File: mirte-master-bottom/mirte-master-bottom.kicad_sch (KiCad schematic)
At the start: 17 parts, among them J13 oled_conn, J23 e-stop, J6 ledstrip, Q1 DMG2305UX, SW2 EM_SWITCH

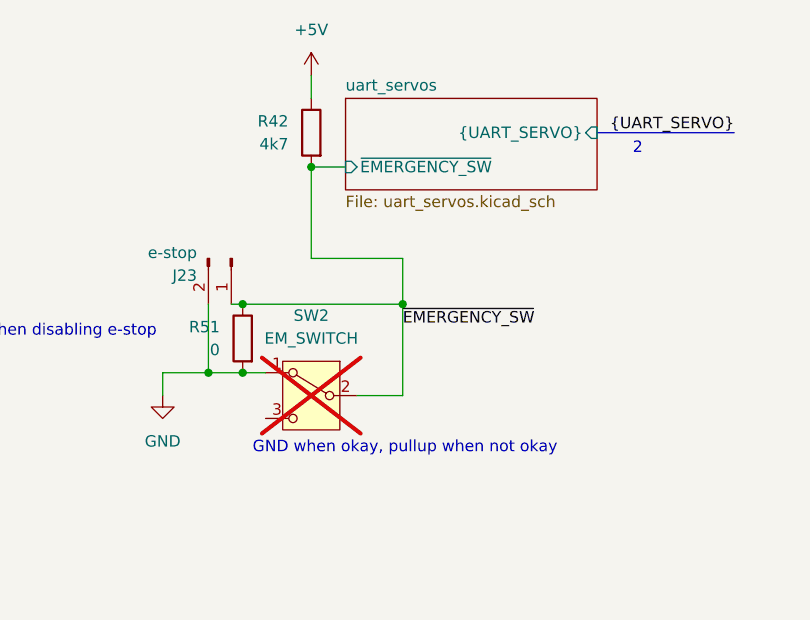
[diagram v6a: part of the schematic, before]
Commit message: change to 12v em switch
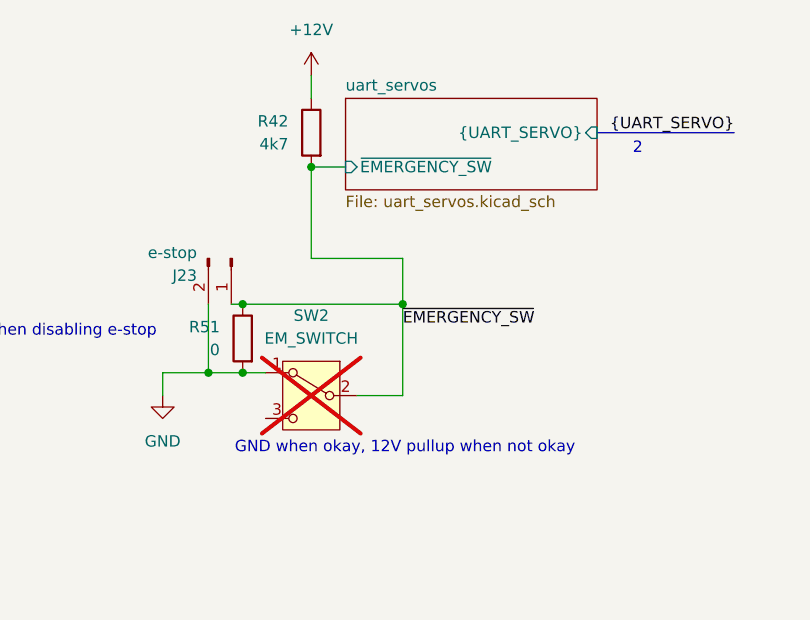
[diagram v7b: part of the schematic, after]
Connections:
- net +12V: now also R42.1
- net +5V: no longer R42.1
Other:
- note added: "GND when okay, 12V pullup when not okay"
- note removed: "GND when okay, pullup when not okay"
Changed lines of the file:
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@@
 		)
 	)
-	(text "GND when okay, pullup when not okay"
+	(text "GND when okay, 12V pullup when not okay"
 		(exclude_from_sim no)
 		(at 48.514 69.342 0)
@@
 				(path "/c479422a-501d-4123-8665-56a1c70bd9ea"
 					(reference "A1")
+					(unit 1)
+				)
+			)
+		)
+	)
+	(symbol
+		(lib_id "power:+12V")
+		(at 38.1 27.94 0)
+		(unit 1)
+		(exclude_from_sim no)
+		(in_bom yes)
+		(on_board yes)
+		(dnp no)
+		(fields_autoplaced yes)
+		(property "Reference" "#PWR62"
+			(at 38.1 31.75 0)
+			(effects
+				(font
+					(size 1.27 1.27)
+				)
+				(hide yes)
+			)
+		)
+		(property "Value" "+12V"
+			(at 38.1 22.86 0)
+			(effects
+				(font
+					(size 1.27 1.27)
+				)
+			)
+		)
+		(property "Footprint" ""
+			(at 38.1 27.94 0)
+			(effects
+				(font
+					(size 1.27 1.27)
+				)
+				(hide yes)
+			)
+		)
+		(property "Datasheet" ""
+			(at 38.1 27.94 0)
+			(effects
+				(font
+					(size 1.27 1.27)
+				)
+				(hide yes)
+			)
+		)
+		(property "Description" "Power symbol creates a global label with name \"+12V\""
+			(at 38.1 27.94 0)
+			(effects
+				(font
+					(size 1.27 1.27)
+				)
+				(hide yes)
+			)
+		)
+		(pin "1"
+		)
+		(instances
+			(project "mirte-master-bottom"
+				(path "/c479422a-501d-4123-8665-56a1c70bd9ea"
+					(reference "#PWR62")
 					(unit 1)
 				)
@@
 					(unit 1)
 				)
-			)
-		)
-	)
-	(symbol
-		(lib_id "power:+5V")
-		(at 38.1 27.94 0)
-		(unit 1)
-		(exclude_from_sim no)
-		(in_bom yes)
-		(on_board yes)
-		(dnp no)
-		(fields_autoplaced yes)
-		(property "Reference" "#PWR61"
-			(at 38.1 31.75 0)
-			(effects
-				(font
-					(size 1.27 1.27)
-				)
-				(hide yes)
-			)
-		)
-		(property "Value" "+5V"
-			(at 38.1 22.86 0)
-			(effects
-				(font
-					(size 1.27 1.27)
-				)
-			)
-		)
-		(property "Footprint" ""
-			(at 38.1 27.94 0)
-			(effects
-				(font
-					(size 1.27 1.27)
-				)
-				(hide yes)
-			)
-		)
-		(property "Datasheet" ""
-			(at 38.1 27.94 0)
-			(effects
-				(font
-					(size 1.27 1.27)
-				)
-				(hide yes)
-			)
-		)
-		(property "Description" "Power symbol creates a global label with name \"+5V\""
-			(at 38.1 27.94 0)
-			(effects
-				(font
-					(size 1.27 1.27)
-				)
-				(hide yes)
-			)
-		)
-		(pin "1"
-		)
-		(instances
-			(project "mirte-master-bottom"
-				(path "/c479422a-501d-4123-8665-56a1c70bd9ea"
-					(reference "#PWR61")
-					(unit 1)
-				)

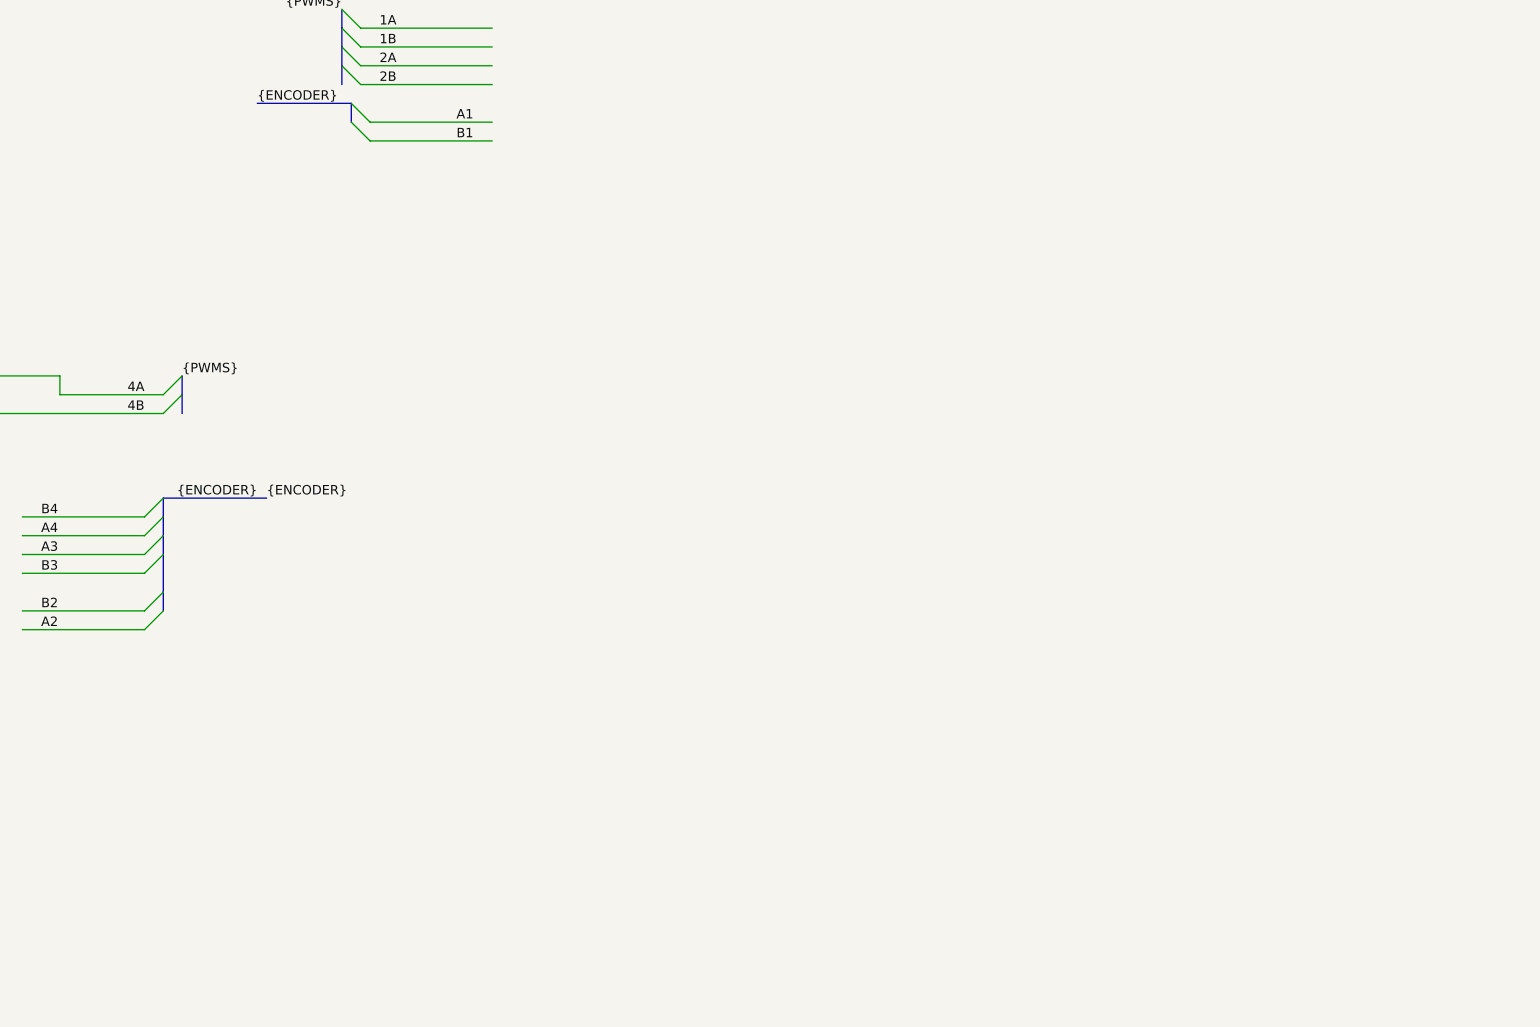
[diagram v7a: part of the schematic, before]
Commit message: Upd, add feetech servo connector
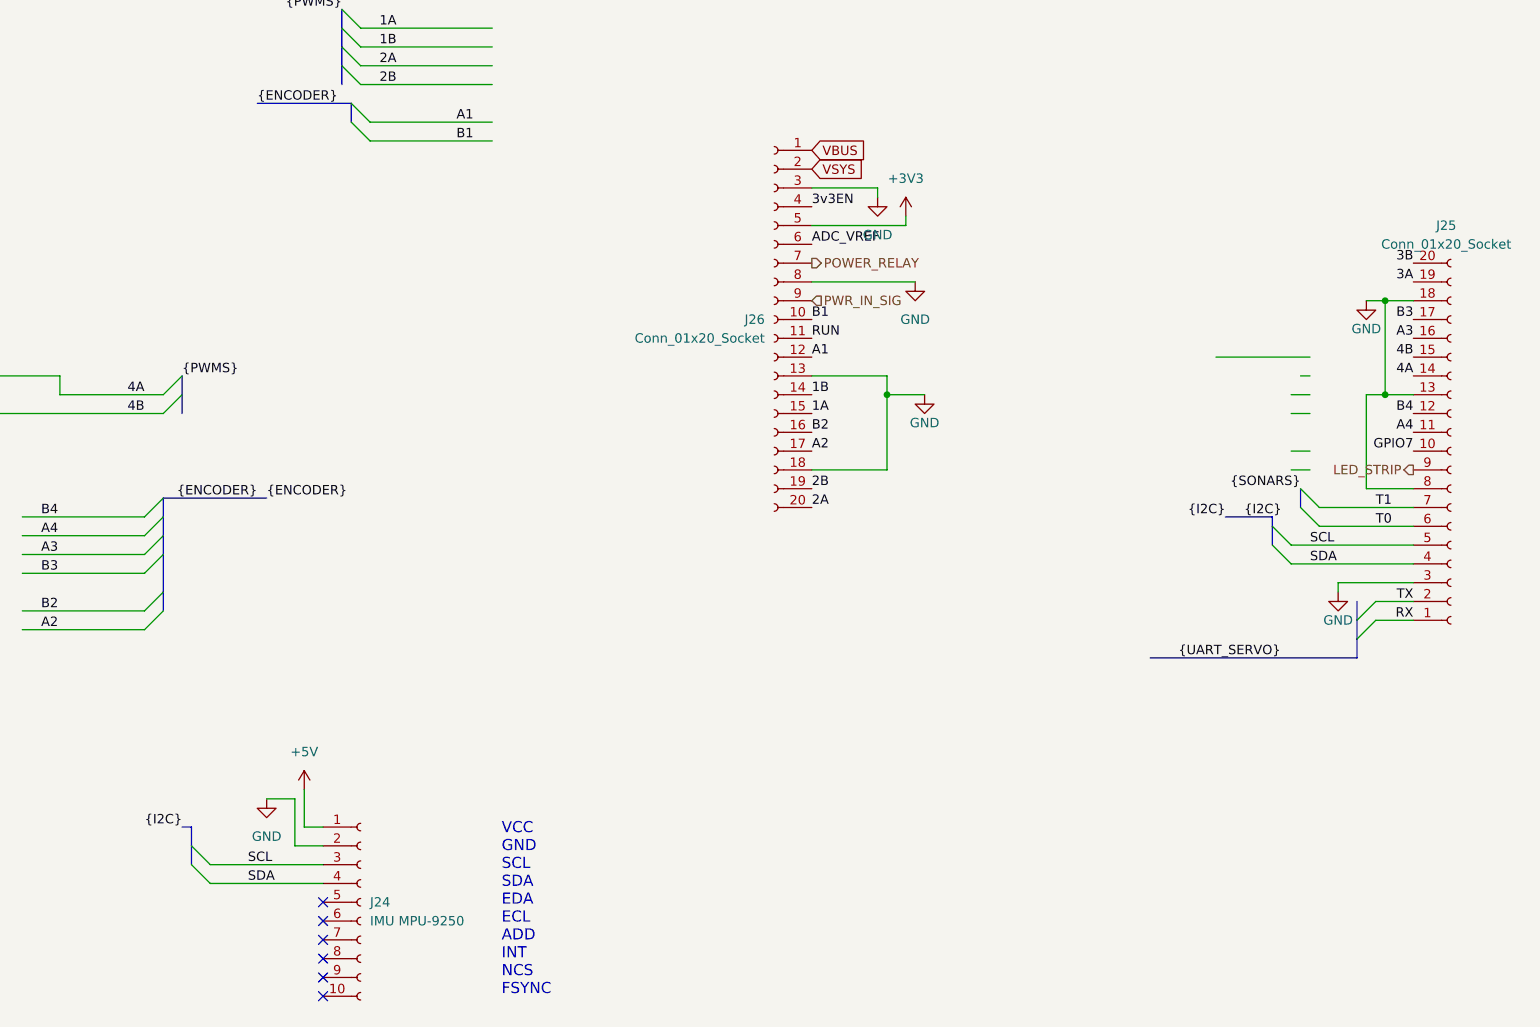
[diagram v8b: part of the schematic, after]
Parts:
- added J24: IMU MPU-9250, Library:MPU9250, symbol Connector:Conn_01x10_Socket
- added J25, J26: Conn_01x20_Socket, Connector_PinHeader_2.54mm:PinHeader_1x20_P2.54mm_Vertical, symbol Connector:Conn_01x20_Socket
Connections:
- net +3V3: now also J26.5 (Pin_5)
- net +5V: now also J24.1 (Pin_1)
- net 1A: now also J26.15 (Pin_15)
- net 1B: now also J26.14 (Pin_14)
- net 2A: now also J26.20 (Pin_20)
- net 2B: now also J26.19 (Pin_19)
- net 3A: now also J25.19 (Pin_19)
- net 3B: now also J25.20 (Pin_20)
- net 3v3EN: now also J26.4 (Pin_4)
- net 4A: now also J25.14 (Pin_14)
- net 4B: now also J25.15 (Pin_15)
- net A1: now also J26.12 (Pin_12)
- net A2: now also J26.17 (Pin_17)
- net A3: now also J25.16 (Pin_16)
- net A4: now also J25.11 (Pin_11)
- net ADC_VREF: now also J26.6 (Pin_6)
- net B1: now also J26.10 (Pin_10)
- net B2: now also J26.16 (Pin_16)
- net B3: now also J25.17 (Pin_17)
- net B4: now also J25.12 (Pin_12)
- net GND: now also J24.2 (Pin_2), J25.13 (Pin_13), J25.18 (Pin_18), J25.3 (Pin_3), J25.8 (Pin_8), J26.13 (Pin_13), J26.18 (Pin_18), J26.3 (Pin_3), J26.8 (Pin_8)
- net GPIO7: now also J25.10 (Pin_10)
- net LED_STRIP: now also J25.9 (Pin_9)
- net POWER_RELAY: now also J26.7 (Pin_7)
- net PWR_IN_SIG: now also J26.9 (Pin_9)
- net RUN: now also J26.11 (Pin_11)
- net RX: now also J25.1 (Pin_1)
- net SCL: now also J24.3 (Pin_3), J25.5 (Pin_5)
- net SDA: now also J24.4 (Pin_4), J25.4 (Pin_4)
- net T0: now also J25.6 (Pin_6)
- net T1: now also J25.7 (Pin_7)
- net TX: now also J25.2 (Pin_2)
- net VBUS: now also J26.1 (Pin_1)
- net VSYS: now also J26.2 (Pin_2)
- no-connect marks 0 -> 6
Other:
- note added: "VCC GND SCL SDA EDA ECL ADD INT NCS FSYNC"
